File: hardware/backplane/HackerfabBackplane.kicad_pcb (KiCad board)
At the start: 4 copper layers, 111.5 x 154 mm, 144 parts, among them J1 9001-12961C00A, J2 9001-12961C00A, J3 9001-12961C00A, J4 KF128-5.08-2P-AA, J5 KF128-5.08-2P-AA, J6 KF128-5.08-2P-AA, J7 TYPE-C-31-M-12, J9 ZX-SH1.0-3PWT, Q1 DMP6023LE-13, U1 TPS5450DDAR, U2 TPS5450DDAR, U3 AP2112K-3.3TRG1, U4 USBLC6-2SC6, U5 RP2354B, U6 TPS2116DRL, U7 W25Q128JVSIQ, Y1 12MHz

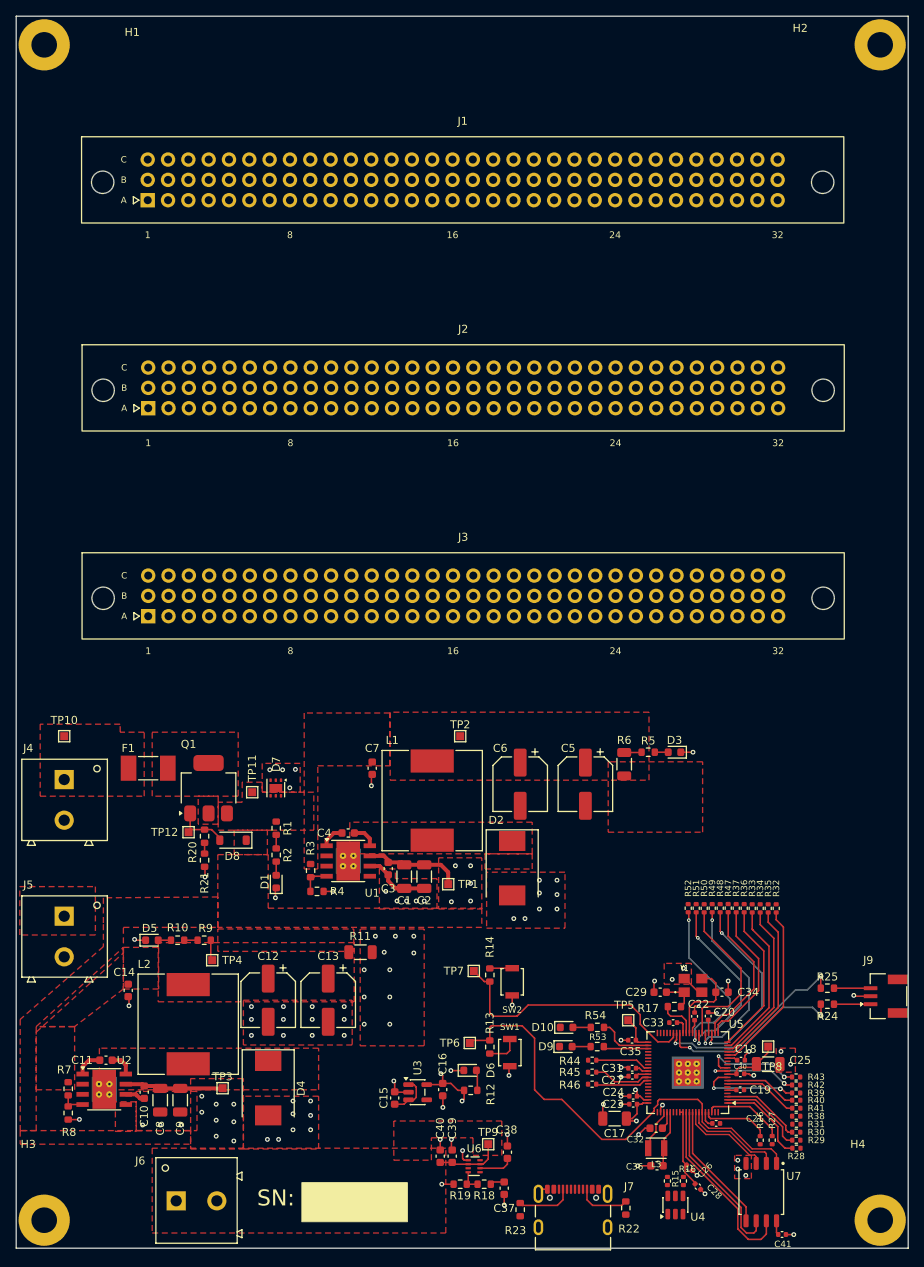
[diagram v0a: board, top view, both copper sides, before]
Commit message: Import October 30 V6 schematic and routing updates
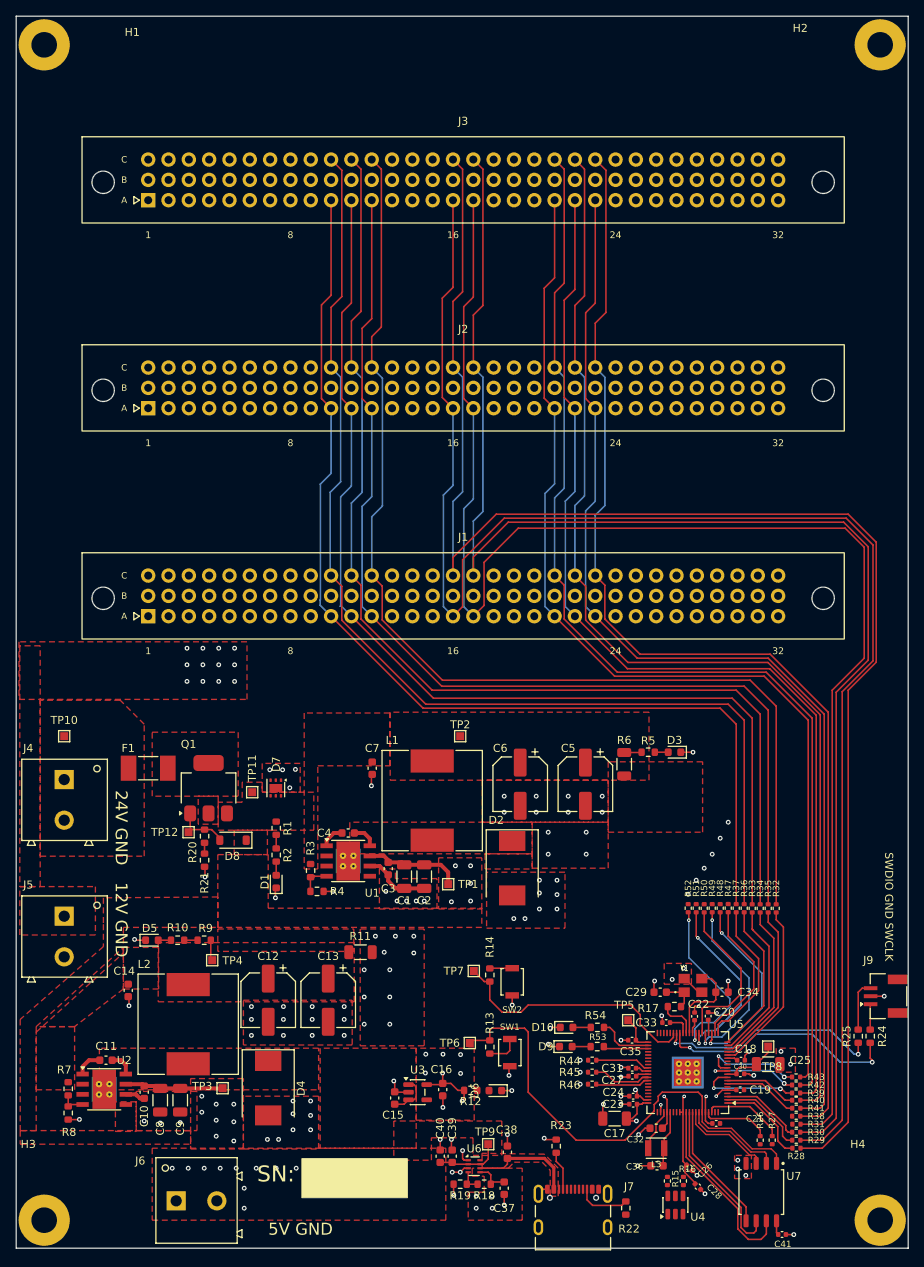
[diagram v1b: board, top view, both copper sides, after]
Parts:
- moved J1 52.0 mm to (62.5, 105.0)
- moved J3 52.0 mm to (62.5, 53.0)
- moved R23 9.12 mm to (113.5, 171.2), turned to 90 degrees
- moved R25 7.13 mm to (151.2, 157.5), turned to 90 degrees
- moved R24 6.68 mm to (152.8, 157.5), turned to 90 degrees
- moved D6 4.04 mm to (105.9, 164.3), turned to 180 degrees
- moved C33 0.87 mm to (127.2, 155.8)
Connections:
- J1 pad A10: unconnected-(J1-PadA10) -> /SPI0_CS3
- J1 pad A11: /AUX1 -> /SPI0_MOSI
- J1 pad A12: unconnected-(J1-PadA12) -> /SPI0_CS1
- J1 pad A14: /AUX2 -> /AUX1
- J1 pad A15: /SPI0_CS3 -> unconnected-(J1-PadA15)
- J1 pad A16: /SPI0_MOSI -> /I2C0_SCL
- J1 pad A17: /SPI0_CS1 -> /I2C1_SCL
- J1 pad A18: /SPI1_CS3 -> unconnected-(J1-PadA18)
- J1 pad A19: /SPI1_MOSI -> /AUX2
- J1 pad A20: /SPI1_CS1 -> /UART_RX
- J1 pad A21: /I2C1_SCL -> /SPI1_CS3
- J1 pad A22: /I2C0_SCL -> /SPI1_MOSI
- J1 pad A23: /UART_RX -> /SPI1_CS1
- J1 pad C10: unconnected-(J1-PadC10) -> /SPI0_CS2
- J1 pad C11: unconnected-(J1-PadC11) -> /SPI0_CLK
- J1 pad C12: unconnected-(J1-PadC12) -> /SPI0_MISO
- J1 pad C13: /AUX3 -> unconnected-(J1-PadC13)
- J1 pad C15: /SPI0_CS2 -> unconnected-(J1-PadC15)
- J1 pad C16: /SPI0_CLK -> /I2C0_SDA
- J1 pad C17: /SPI0_MISO -> /I2C1_SDA
- J1 pad C18: /SPI1_CS2 -> /AUX3
- J1 pad C19: /SPI1_CLK -> unconnected-(J1-PadC19)
- J1 pad C20: /SPI1_MISO -> /UART_TX
- J1 pad C21: /I2C1_SDA -> /SPI1_CS2
- J1 pad C22: /I2C0_SDA -> /SPI1_CLK
- J1 pad C23: /UART_TX -> /SPI1_MISO
- J2 pad A10: unconnected-(J2-PadA10) -> /SPI0_CS3
- J2 pad A11: unconnected-(J2-PadA11) -> /SPI0_MOSI
- J2 pad A12: unconnected-(J2-PadA12) -> /SPI0_CS1
- J2 pad A13: /AUX5 -> unconnected-(J2-PadA13)
- J2 pad A15: /SPI0_CS3 -> unconnected-(J2-PadA15)
- J2 pad A16: /SPI0_MOSI -> /I2C0_SCL
- J2 pad A17: /SPI0_CS1 -> /I2C1_SCL
- J2 pad A18: /SPI1_CS3 -> /AUX5
- J2 pad A19: /SPI1_MOSI -> unconnected-(J2-PadA19)
- J2 pad A20: /SPI1_CS1 -> unconnected-(J2-PadA20)
- J2 pad A21: /I2C1_SCL -> /SPI1_CS3
- J2 pad A22: /I2C0_SCL -> /SPI1_MOSI
- J2 pad A23: unconnected-(J2-PadA23) -> /SPI1_CS1
- J2 pad C10: /AUX4 -> /SPI0_CS2
- J2 pad C11: unconnected-(J2-PadC11) -> /SPI0_CLK
- J2 pad C12: /AUX6 -> /SPI0_MISO
- J2 pad C13: unconnected-(J2-PadC13) -> /AUX4
- J2 pad C15: /SPI0_CS2 -> /AUX6
- J2 pad C16: /SPI0_CLK -> /I2C0_SDA
- J2 pad C17: /SPI0_MISO -> /I2C1_SDA
- J2 pad C18: /SPI1_CS2 -> unconnected-(J2-PadC18)
- J2 pad C19: /SPI1_CLK -> unconnected-(J2-PadC19)
- J2 pad C20: /SPI1_MISO -> unconnected-(J2-PadC20)
- J2 pad C21: /I2C1_SDA -> /SPI1_CS2
- J2 pad C22: /I2C0_SDA -> /SPI1_CLK
- J2 pad C23: unconnected-(J2-PadC23) -> /SPI1_MISO
- J3 pad A10: /AUX7 -> /SPI0_CS3
- J3 pad A11: unconnected-(J3-PadA11) -> /SPI0_MOSI
- J3 pad A12: /AUX8 -> /SPI0_CS1
- J3 pad A13: unconnected-(J3-PadA13) -> /AUX7
- J3 pad A15: /SPI0_CS3 -> /AUX8
- J3 pad A16: /SPI0_MOSI -> /I2C0_SCL
- J3 pad A17: /SPI0_CS1 -> /I2C1_SCL
- J3 pad A18: /SPI1_CS3 -> unconnected-(J3-PadA18)
- J3 pad A19: /SPI1_MOSI -> unconnected-(J3-PadA19)
- J3 pad A20: /SPI1_CS1 -> unconnected-(J3-PadA20)
- J3 pad A21: /I2C1_SCL -> /SPI1_CS3
- J3 pad A22: /I2C0_SCL -> /SPI1_MOSI
- J3 pad A23: /UART_RX -> /SPI1_CS1
- J3 pad C10: unconnected-(J3-PadC10) -> /SPI0_CS2
- J3 pad C11: /AUX9 -> /SPI0_CLK
- J3 pad C12: unconnected-(J3-PadC12) -> /SPI0_MISO
- J3 pad C14: /AUX10 -> /AUX9
- J3 pad C15: /SPI0_CS2 -> unconnected-(J3-PadC15)
- J3 pad C16: /SPI0_CLK -> /I2C0_SDA
- J3 pad C17: /SPI0_MISO -> /I2C1_SDA
- J3 pad C18: /SPI1_CS2 -> unconnected-(J3-PadC18)
- J3 pad C19: /SPI1_CLK -> /AUX10
- J3 pad C20: /SPI1_MISO -> unconnected-(J3-PadC20)
- J3 pad C21: /I2C1_SDA -> /SPI1_CS2
- J3 pad C22: /I2C0_SDA -> /SPI1_CLK
- J3 pad C23: unconnected-(J3-PadC23) -> /SPI1_MISO
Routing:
- net /I2C0_SCL: track 0.00 -> 196.3 mm
- net /I2C0_SDA: track 0.00 -> 194.1 mm
- net /I2C1_SCL: track 0.00 -> 188.6 mm
- net /I2C1_SDA: track 0.00 -> 187.0 mm
- net /SPI1_MISO: track 0.00 -> 146.2 mm
- net /SPI1_CLK: track 0.00 -> 144.7 mm
- net /SPI1_CS2: track 0.00 -> 143.2 mm
- net /SPI1_CS1: track 0.00 -> 139.6 mm
- net /SPI0_CS2: track 0.00 -> 138.8 mm
- net /SPI0_MISO: track 0.00 -> 138.7 mm
- net /SPI0_CLK: track 0.00 -> 138.6 mm
- net /SPI1_MOSI: track 0.00 -> 138.4 mm
- net /SPI1_CS3: track 0.00 -> 136.6 mm
- net /SPI0_MOSI: track 0.00 -> 132.9 mm
- net /SPI0_CS3: track 0.00 -> 132.8 mm
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- added copper zone on F.Cu, net +3V3
- added copper zone on F.Cu, net +5V_USB
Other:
- board text added: "12V GND"
- board text added: "24V GND"
- board text added: "5V GND"
- board text added: "SWDIO GND SWCLK"
